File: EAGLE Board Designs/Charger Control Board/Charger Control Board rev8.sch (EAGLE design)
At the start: 115 parts, among them K1 RELAY_DPDT, K2 RELAY_DPDT, K3 RELAY_DPDT, U1 LOGICGATE_BUFFER, U100 MCP2562FD, U101 MCP2562FD, U2 ADM8316WBX30, U3 VOLTAGE_REGULATOR_MODULE_OKI-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

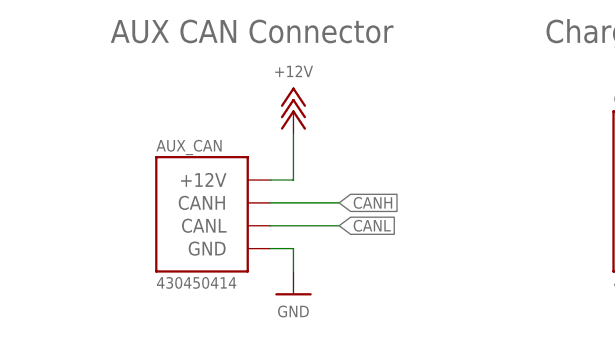
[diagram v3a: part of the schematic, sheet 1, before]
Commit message: Fixed missing BOM part numbers
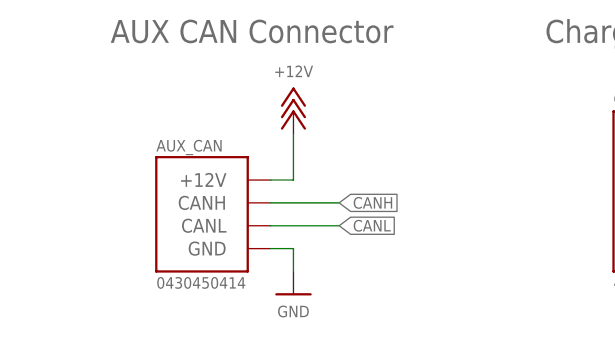
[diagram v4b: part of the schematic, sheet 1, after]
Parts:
- AUX_CAN: value CONNECTOR-CAN_MF_T_V_ -> CONNECTOR-CAN_MF_T_V_BLACK; device HyTechDevices - Copy:CONNECTOR-CAN_MF_T_V_ -> HyTechDevices_temp:CONNECTOR-CAN_MF_T_V_BLACK
- CHG_CAN: value CONNECTOR-6_MF_T_V_ -> CONNECTOR-6_MF_T_V_BLACK; device HyTechDevices - Copy:CONNECTOR-6_MF_T_V_ -> HyTechDevices:CONNECTOR-6_MF_T_V_BLACK
- MAIN_CONNECTOR: value CONNECTOR-8_MF_T_V_ -> CONNECTOR-8_MF_T_V_BLACK; device HyTechDevices - Copy:CONNECTOR-8_MF_T_V_ -> HyTechDevices:CONNECTOR-8_MF_T_V_BLACK
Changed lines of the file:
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@@
 <part name="C6" library="HyTechDevices" deviceset="CAPACITOR_?_*" device="0603" technology="25V_10UF"/>
 <part name="P5" library="HyTechSupplies" deviceset="GND" device=""/>
-<part name="MAIN_CONNECTOR" library="HyTechDevices - Copy" deviceset="CONNECTOR-8_?_*" device="MF_T_V"/>
+<part name="MAIN_CONNECTOR" library="HyTechDevices" deviceset="CONNECTOR-8_?_*" device="MF_T_V" technology="BLACK"/>
 <part name="P6" library="HyTechSupplies" deviceset="+12V" device=""/>
 <part name="P7" library="HyTechSupplies" deviceset="GND" device=""/>
@@
 <part name="C5" library="HyTechDevices" deviceset="CAPACITOR_?_*" device="0603" technology="10V_1UF"/>
 <part name="C4" library="HyTechDevices" deviceset="CAPACITOR_?_*" device="0603" technology="10V_0.1UF"/>
-<part name="AUX_CAN" library="HyTechDevices - Copy" deviceset="CONNECTOR-CAN_?_*" device="MF_T_V"/>
+<part name="AUX_CAN" library="HyTechDevices_temp" deviceset="CONNECTOR-CAN_?_*" device="MF_T_V" technology="BLACK"/>
 <part name="P57" library="HyTechSupplies" deviceset="+12V" device=""/>
 <part name="P58" library="HyTechSupplies" deviceset="GND" device=""/>
@@
 <part name="R31" library="HyTechDevices" deviceset="RESISTOR_?_*" device="0603" technology="240"/>
 <part name="P15" library="HyTechSupplies" deviceset="GND" device=""/>
-<part name="CHG_CAN" library="HyTechDevices - Copy" deviceset="CONNECTOR-6_?_*" device="MF_T_V"/>
+<part name="CHG_CAN" library="HyTechDevices" deviceset="CONNECTOR-6_?_*" device="MF_T_V" technology="BLACK"/>
 <part name="P56" library="HyTechSupplies" deviceset="GND" device=""/>
 <part name="R18" library="HyTechDevices" deviceset="RESISTOR_?_*" device="0603" technology="33K" value="RESISTOR_0603_33K"/>

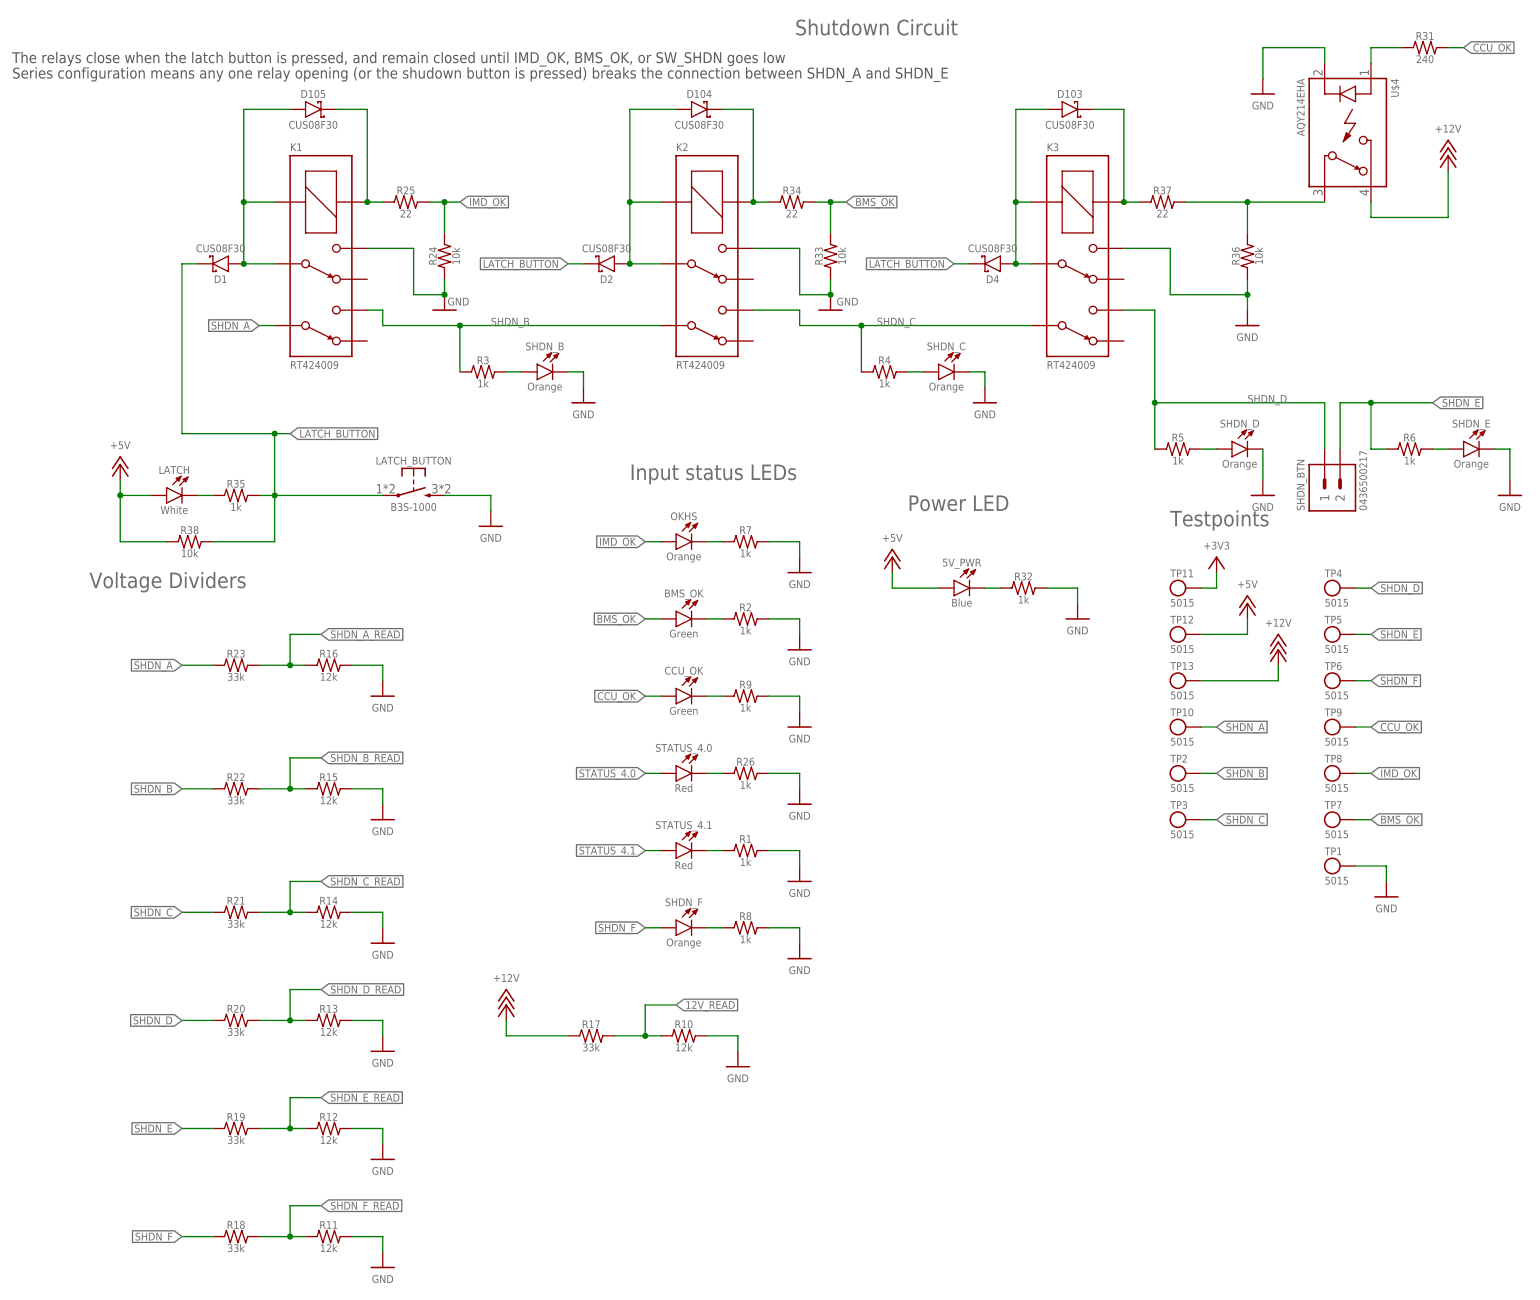
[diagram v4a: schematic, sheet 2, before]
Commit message: Fixed fonts
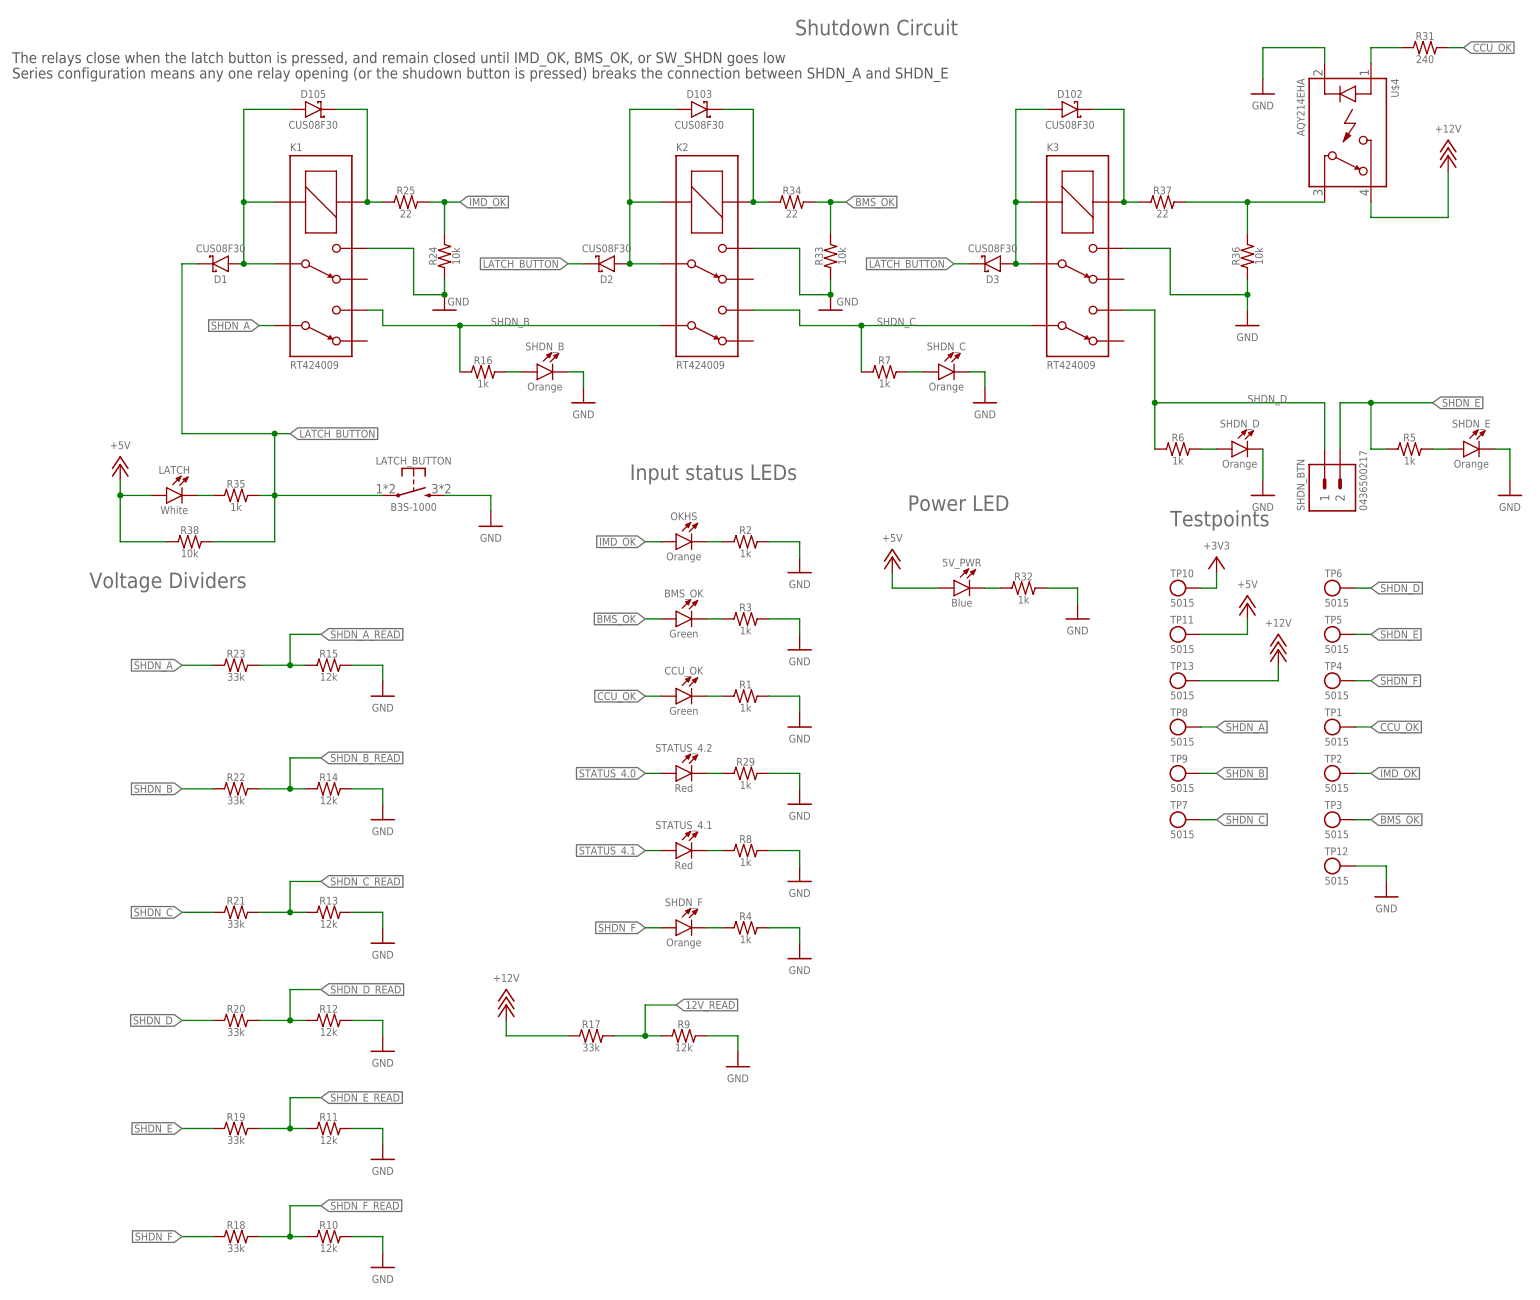
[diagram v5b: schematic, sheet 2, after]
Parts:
- removed D5: TVS_15V, HyTechDevices:TVS_15V
- added D3: SCHOTTKY_SOD323_30V, HyTechDevices:SCHOTTKY_SOD323_30V
- C10: value CAPACITOR_0603_10V_0.1UF -> CAPACITOR_0603_10V_4.7NF; device HyTechDevices:CAPACITOR_0603_10V_0.1UF -> HyTechDevices:CAPACITOR_0603_10V_4.7NF
- C7: value CAPACITOR_0603_25V_10UF -> CAPACITOR_0603_10V_0.1UF; device HyTechDevices:CAPACITOR_0603_25V_10UF -> HyTechDevices:CAPACITOR_0603_10V_0.1UF
- C8: value CAPACITOR_0603_10V_4.7NF -> CAPACITOR_0603_10V_1UF; device HyTechDevices:CAPACITOR_0603_10V_4.7NF -> HyTechDevices:CAPACITOR_0603_10V_1UF
- C9: value CAPACITOR_0603_10V_1UF -> CAPACITOR_0603_25V_10UF; device HyTechDevices:CAPACITOR_0603_10V_1UF -> HyTechDevices:CAPACITOR_0603_25V_10UF
- D100: value TVS_BIDIRECTIONAL_DUAL -> TVS_15V; device HyTechDevices:TVS_BIDIRECTIONAL_DUAL -> HyTechDevices:TVS_15V
- D102: value TVS_15V -> SCHOTTKY_SOD323_30V; device HyTechDevices:TVS_15V -> HyTechDevices:SCHOTTKY_SOD323_30V
- D104: value SCHOTTKY_SOD323_30V -> TVS_BIDIRECTIONAL_DUAL; device HyTechDevices:SCHOTTKY_SOD323_30V -> HyTechDevices:TVS_BIDIRECTIONAL_DUAL
- D4: value SCHOTTKY_SOD323_30V -> TVS_15V; device HyTechDevices:SCHOTTKY_SOD323_30V -> HyTechDevices:TVS_15V
- R16: value RESISTOR_0603_12K -> RESISTOR_0603_1K; device HyTechDevices:RESISTOR_0603_12K -> HyTechDevices:RESISTOR_0603_1K
- R26: value RESISTOR_0603_1K -> RESISTOR_0603_100K; device HyTechDevices:RESISTOR_0603_1K -> HyTechDevices:RESISTOR_0603_100K
- R27: value RESISTOR_0603_100K -> RESISTOR_0603_10K; device HyTechDevices:RESISTOR_0603_100K -> HyTechDevices:RESISTOR_0603_10K
- R29: value RESISTOR_0603_10K -> RESISTOR_0603_1K; device HyTechDevices:RESISTOR_0603_10K -> HyTechDevices:RESISTOR_0603_1K
- R9: value RESISTOR_0603_1K -> RESISTOR_0603_12K; device HyTechDevices:RESISTOR_0603_1K -> HyTechDevices:RESISTOR_0603_12K
- TP1: SIGNAL GND -> CCU_OK
- TP10: SIGNAL SHDN_A -> +3V3
- TP11: SIGNAL +3V3 -> +5V
- TP12: SIGNAL +5V -> GND
- TP2: SIGNAL SHDN_B -> IMD_OK
- TP3: SIGNAL SHDN_C -> BMS_OK
- TP4: SIGNAL SHDN_D -> SHDN_F
- TP6: SIGNAL SHDN_F -> SHDN_D
- TP7: SIGNAL BMS_OK -> SHDN_C
- TP8: SIGNAL IMD_OK -> SHDN_A
- TP9: SIGNAL CCU_OK -> SHDN_B
- renumbered STATUS_4.0 to STATUS_4.2, U$100 to U102
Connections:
- net +12V: now also C7.2, C8.1; no longer C10.2, C7.1
- net +3V3: now also TP10.1; no longer TP11.1
- net +5V: now also TP11.1; no longer TP12.1
- net 12V_READ: now also R9.1; no longer R10.1
- net BMS_OK: now also D100.C, TP3.1; no longer D101.C, TP7.1
- net CANH: now also D104.C1; no longer D100.C1
- net CANL: now also D104.C2; no longer D100.C2
- net CCU_OK: now also TP1.1; no longer TP9.1
- net GND: now also C10.2, C7.1, D104.A, D4.A, R28.1, R29.2, R3.2, R4.2, TP12.1; no longer C10.1, C7.2, D102.A, D5.A, R16.2, R28.2, R29.1, R7.2, TP1.1
- net IMD_OK: now also D101.C, TP2.1; no longer D102.C, TP8.1
- net LATCH_BUTTON: now also D3.C; no longer D4.C
- net N$1: now also D4.C; no longer D5.C
- net N$13: now also D103.C; no longer D104.C
- net N$14: now also D103.A; no longer D104.A
- net N$15: now also D102.C; no longer D103.C
- net N$18: now also R6.2; no longer R5.2
- net N$19: now also R5.2; no longer R6.2
- net N$2: now also R26.1; no longer R27.1
- net N$20: now also D102.A, D3.A; no longer D103.A, D4.A
- net N$22: now also R7.2; no longer R4.2
- net N$23: now also R16.2; no longer R3.2
- net N$29: now also R2.1; no longer R7.1
- net N$3: now also R4.1; no longer R8.1
- net N$30: now also R3.1; no longer R2.1
- net N$31: now also R1.1; no longer R9.1
- net N$33: now also R29.1; no longer R26.1
- net N$39: now also R8.1; no longer R1.1
- net N$9: now also C10.1; no longer C8.1
- net SHDN_A: now also TP8.1; no longer TP10.1
- net SHDN_A_READ: now also R15.1; no longer R16.1
- net SHDN_B: now also R16.1, TP9.1; no longer R3.1, TP2.1
- net SHDN_B_READ: now also R14.1; no longer R15.1
- net SHDN_C: now also R7.1, TP7.1; no longer R4.1, TP3.1
- net SHDN_C_READ: now also R13.1; no longer R14.1
- net SHDN_D: now also R6.1, TP6.1; no longer R5.1, TP4.1
- net SHDN_D_READ: now also R12.1; no longer R13.1
- net SHDN_E: now also R5.1; no longer R6.1
- net SHDN_E_READ: now also R11.1; no longer R12.1
- net SHDN_F: now also TP4.1; no longer TP6.1
- net SHDN_F_READ: now also R10.1; no longer R11.1
- net SW_SHUTDOWN: now also R28.2; no longer R29.2
- net WATCHDOG_IN: now also R27.1; no longer R28.1
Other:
- moved on the sheet: C10, C7, C8, C9, D101, D103, R1, R10, R11, R12, R13, R14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
